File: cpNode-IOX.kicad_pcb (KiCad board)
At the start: 2 copper layers, 110 x 68.5 mm, 66 parts, among them J1 CON_1x04-0.100-screw, J10 Conn_01x02, J11 CON_1x04-0.100-screw, J12 CON_1x04-0.100-screw, J13 Conn_01x08, J14 Conn_01x08, J15 CON_1x04-0.100-screw, J16 CON_1x04-0.100-screw, J17 Conn_01x08, J18 Conn_01x08, J19 Conn_01x02, J2 CON_1x04-0.100-screw, J3 Conn_01x02, J4 Vin, J5 Vout, J6 DCJ0202, J7 Conn_01x02, J8 Conn_01x02, J9 Conn_01x02, Q1 Q_P-FET_8A_SOP-8_A04443, U1 MCP23017_SO, U2 74HC4511D,653, U3 ARKLED SM420561N

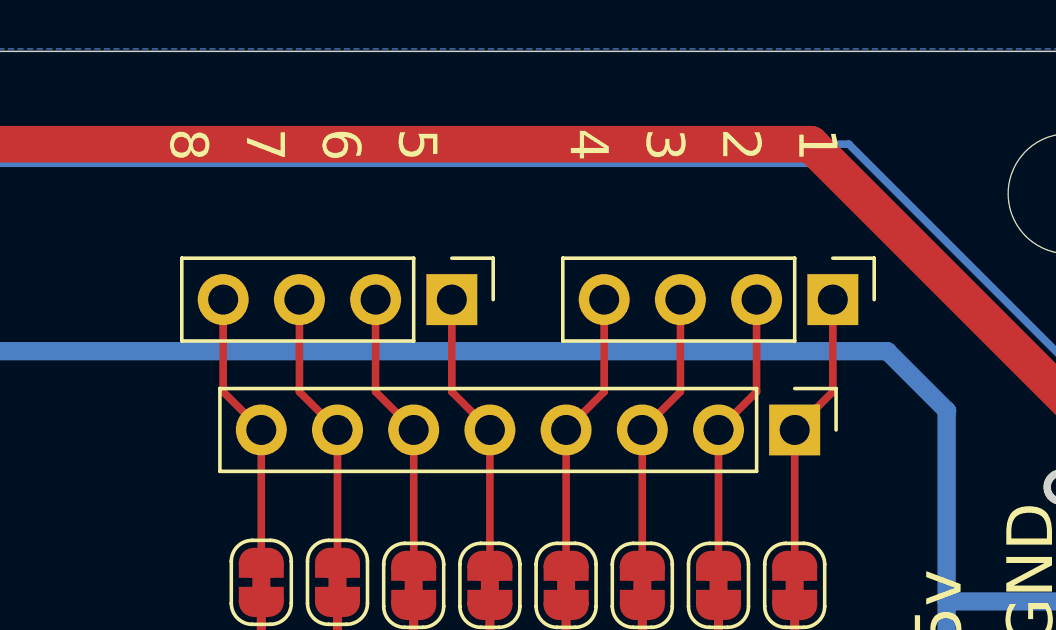
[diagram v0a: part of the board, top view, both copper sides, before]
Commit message: fix:align connectors
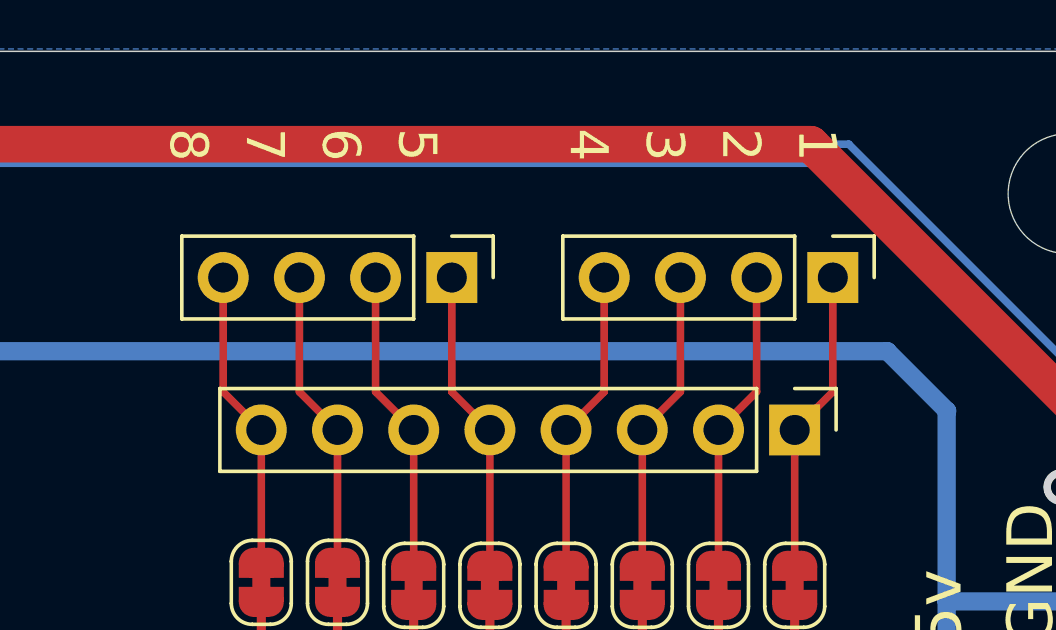
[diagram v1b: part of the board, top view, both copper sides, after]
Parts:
- moved J15 0.73 mm to (224.2, 66.0)
- moved J16 0.73 mm to (211.5, 66.0)
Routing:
- net Net-(J16-Pin_3): track 9.30 -> 9.94 mm
- net Net-(J16-Pin_4): track 9.30 -> 9.94 mm
- net Net-(J16-Pin_2): track 9.40 -> 10.0 mm
- net Net-(J16-Pin_1): track 9.40 -> 10.0 mm
- net Net-(J15-Pin_4): track 9.40 -> 10.0 mm
- net Net-(J15-Pin_3): track 9.40 -> 10.0 mm
- net Net-(J15-Pin_2): track 9.40 -> 10.0 mm
- net Net-(J15-Pin_1): track 9.40 -> 10.0 mm
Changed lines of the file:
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@@
 	(footprint "Connector_PinHeader_2.54mm:PinHeader_1x04_P2.54mm_Vertical"
 		(layer "F.Cu")
-		(at 211.455 66.775 -90)
+		(at 211.455 66.04 -90)
 		(descr "Through hole straight pin header, 1x04, 2.54mm pitch, single row")
 		(tags "Through hole pin header THT 1x04 2.54mm single row")
@@
 	(footprint "Connector_PinHeader_2.54mm:PinHeader_1x04_P2.54mm_Vertical"
 		(layer "F.Cu")
-		(at 224.155 66.775 -90)
+		(at 224.155 66.04 -90)
 		(descr "Through hole straight pin header, 1x04, 2.54mm pitch, single row")
 		(tags "Through hole pin header THT 1x04 2.54mm single row")
@@
 	)
 	(segment
-		(start 221.615 66.775)
-		(end 221.615 69.85)
+		(start 221.615 69.85)
+		(end 220.345 71.12)
 		(width 0.254)
 		(layer "F.Cu")
@@
 	)
 	(segment
-		(start 221.615 69.85)
-		(end 220.345 71.12)
+		(start 221.615 66.14)
+		(end 221.615 69.85)
 		(width 0.254)
 		(layer "F.Cu")
@@
 	)
 	(segment
-		(start 208.915 69.85)
-		(end 208.915 66.775)
+		(start 210.185 75.65)
+		(end 210.185 71.12)
 		(width 0.254)
 		(layer "F.Cu")
@@
 	)
 	(segment
-		(start 210.185 75.65)
-		(end 210.185 71.12)
+		(start 208.915 69.85)
+		(end 208.915 66.14)
 		(width 0.254)
 		(layer "F.Cu")
@@
 	)
 	(segment
-		(start 219.075 69.85)
-		(end 217.805 71.12)
+		(start 219.075 66.14)
+		(end 219.075 69.85)
 		(width 0.254)
 		(layer "F.Cu")
@@
 	)
 	(segment
-		(start 219.075 66.775)
-		(end 219.075 69.85)
+		(start 219.075 69.85)
+		(end 217.805 71.12)
 		(width 0.254)
 		(layer "F.Cu")
@@
 	)
 	(segment
-		(start 211.455 69.85)
-		(end 211.455 66.775)
+		(start 212.725 71.12)
+		(end 211.455 69.85)
 		(width 0.254)
 		(layer "F.Cu")
@@
 	)
 	(segment
-		(start 212.725 75.65)
-		(end 212.725 71.12)
+		(start 211.455 69.85)
+		(end 211.455 66.14)
 		(width 0.254)
 		(layer "F.Cu")
@@
 	)
 	(segment
-		(start 212.725 71.12)
-		(end 211.455 69.85)
+		(start 212.725 75.65)
+		(end 212.725 71.12)
 		(width 0.254)
 		(layer "F.Cu")
@@
 	)
 	(segment
-		(start 224.155 66.775)
+		(start 224.155 66.14)
 		(end 224.155 69.85)
 		(width 0.254)
@@
 	(segment
 		(start 206.375 69.85)
-		(end 206.375 66.775)
+		(end 206.375 66.14)
 		(width 0.254)
 		(layer "F.Cu")
@@
 	)
 	(segment
-		(start 207.645 71.12)
-		(end 206.375 69.85)
+		(start 207.645 75.55)
+		(end 207.645 71.12)
 		(width 0.254)
 		(layer "F.Cu")
@@
 	)
 	(segment
-		(start 207.645 75.55)
-		(end 207.645 71.12)
+		(start 207.645 71.12)
+		(end 206.375 69.85)
 		(width 0.254)
 		(layer "F.Cu")
@@
 	(segment
 		(start 203.835 69.85)
-		(end 203.835 66.775)
+		(end 203.835 66.14)
 		(width 0.254)
 		(layer "F.Cu")
@@
 	)
 	(segment
-		(start 216.535 69.85)
-		(end 215.265 71.12)
+		(start 216.535 66.14)
+		(end 216.535 69.85)
 		(width 0.254)
 		(layer "F.Cu")
@@
 	)
 	(segment
-		(start 216.535 66.775)
-		(end 216.535 69.85)
+		(start 216.535 69.85)
+		(end 215.265 71.12)
 		(width 0.254)
 		(layer "F.Cu")

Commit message: moved screw connectors
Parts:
- J1, J11, J12, J15, J16, J2: footprint Connector_PinHeader_2.54mm:PinHeader_1x04_P2.54mm_Vertical -> TerminalBlock_Phoenix:TerminalBlock_Phoenix_MPT-0,5-4-2.54_1x04_P2.54mm_Horizontal
- U2: value 74HC4511D,653 -> IC_SOIC-16_74HC4511
- moved J7 14.6 mm to (141.6, 70.6)
- moved J1 7.71 mm to (146.7, 64.9), turned to 180 degrees
- moved J2 7.71 mm to (159.4, 64.9), turned to 180 degrees
- moved J3 3.61 mm to (154.3, 70.6)
- moved J12 1.27 mm to (175.3, 64.9), turned to 180 degrees
- moved J11 1.17 mm to (188.6, 64.9), turned to 180 degrees
- moved J15 1.17 mm to (224.2, 64.9), turned to 180 degrees
- moved J16 1.17 mm to (211.5, 64.9), turned to 180 degrees
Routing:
- net +5V: track 291.5 -> 300.9 mm
- net SCL: track 210.2 -> 212.3 mm
- net SDA: track 221.4 -> 223.1 mm
- net Net-(J16-Pin_4): track 9.94 -> 11.2 mm
- net Net-(J16-Pin_1): track 10.0 -> 11.3 mm
- net Net-(J15-Pin_4): track 10.0 -> 11.3 mm
- net Net-(J15-Pin_3): track 10.0 -> 11.3 mm
- net Net-(J15-Pin_2): track 10.0 -> 11.3 mm
- net Net-(J12-Pin_4): track 9.94 -> 11.2 mm
- net Net-(J12-Pin_3): track 9.94 -> 11.2 mm
- net Net-(J12-Pin_2): track 9.94 -> 11.2 mm
- net Net-(J12-Pin_1): track 9.94 -> 11.2 mm
- net Net-(J16-Pin_3): track 9.94 -> 11.2 mm
- net Net-(J16-Pin_2): track 10.0 -> 11.3 mm
- net Net-(J15-Pin_1): track 10.0 -> 11.3 mm
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
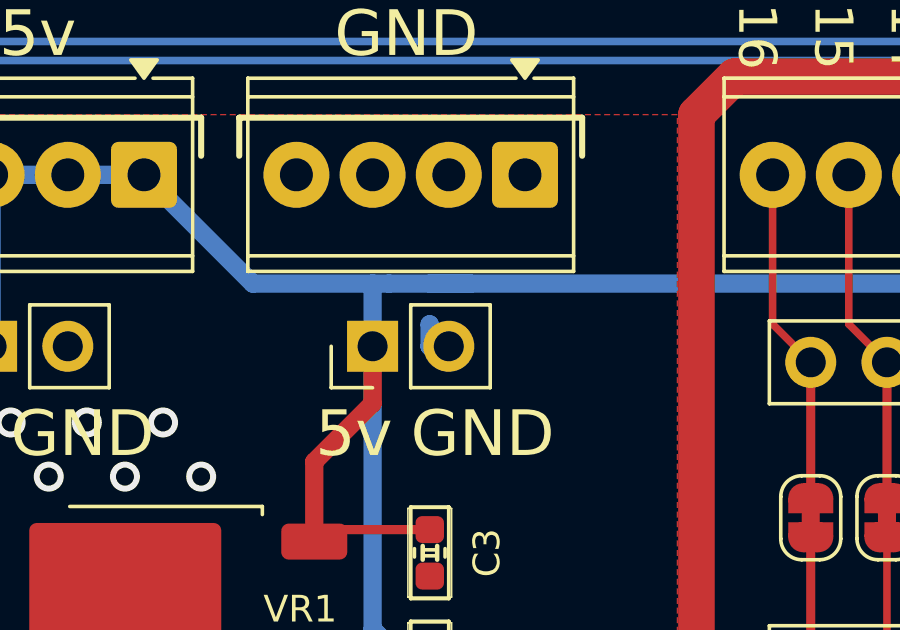
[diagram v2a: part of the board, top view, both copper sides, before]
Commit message: fixed no-impact DRC warning
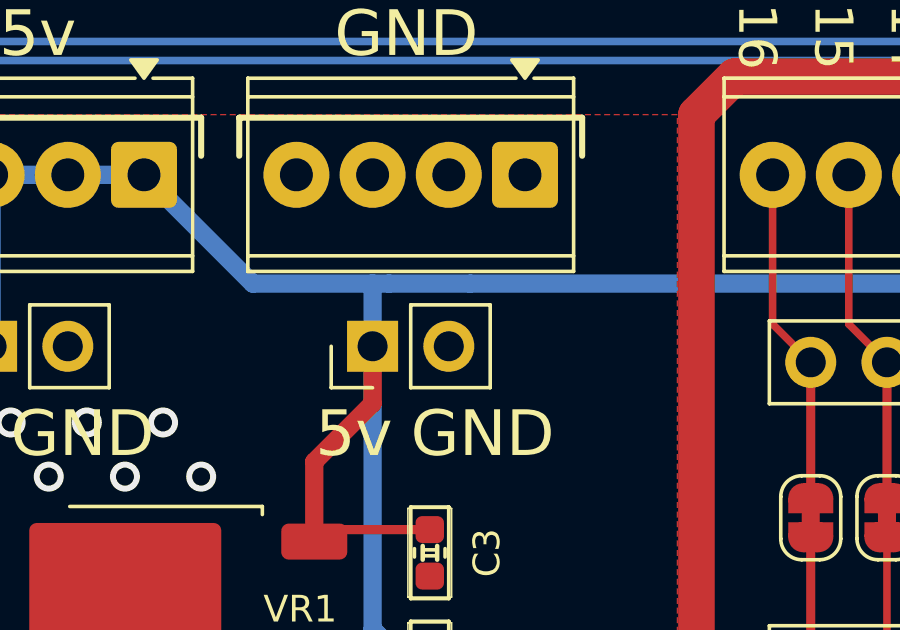
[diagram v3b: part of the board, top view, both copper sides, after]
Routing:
- net +5V: track 300.9 -> 299.5 mm
- net GND: track 37.7 -> 37.0 mm
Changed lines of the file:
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@@
-	)
-	(segment
-		(start 156.21 68.4952)
-		(end 157.5648 68.4952)
-		(width 0.6096)
-		(layer "B.Cu")
-		(net "+5V")
 	)
 	(segment
@@
 		(net "GND")
 	)
-	(segment
-		(start 156.21 70.585)
-		(end 156.205 70.58)
-		(width 0.6096)
-		(layer "B.Cu")
-		(net "GND")
-	)
-	(segment
-		(start 156.205 69.855)
-		(end 156.21 69.85)
-		(width 0.6096)
-		(layer "B.Cu")
-		(net "GND")
-	)
-	(segment
-		(start 156.205 70.59)
-		(end 156.21 70.585)
-		(width 0.6096)
-		(layer "B.Cu")
-		(net "GND")
-	)
-	(segment
-		(start 156.205 70.58)
-		(end 156.205 69.855)
-		(width 0.6096)
-		(layer "B.Cu")
-		(net "GND")
-	)
